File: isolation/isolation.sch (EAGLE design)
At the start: 81 parts, among them IC1 XTLV61048DBVR, IC2 SN74HC14DRG3, IC3 SN74HCS32PWR, IC4 SN74HCS08DYYR, IC5 FDN359BN, IC6 FDN359BN, IC7 FDN359BN, IC8 FDN359BN, J1 S4B-PH-K-S(LF)(SN), J2 S4B-PH-K-S(LF)(SN), J3 S4B-PH-K-S(LF)(SN), J4 S4B-PH-K-S(LF)(SN), J5 S4B-PH-K-S(LF)(SN)

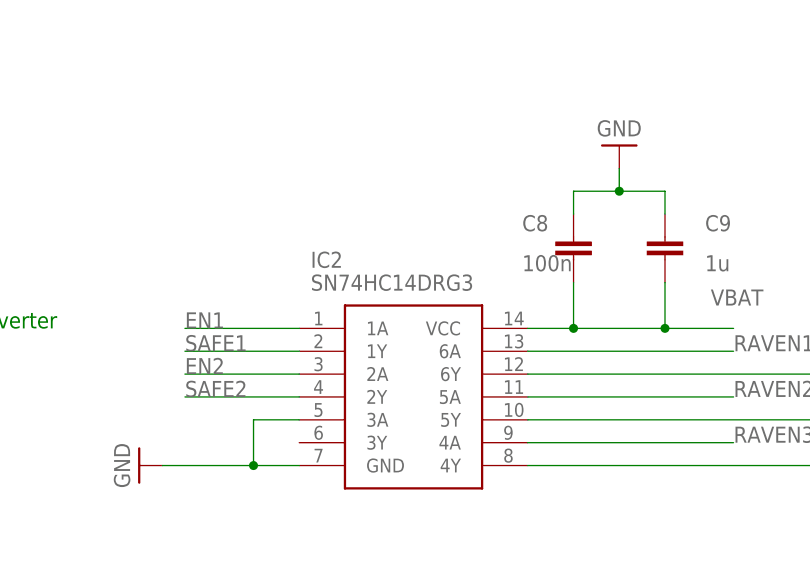
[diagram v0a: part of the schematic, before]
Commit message: move to smaller inverter
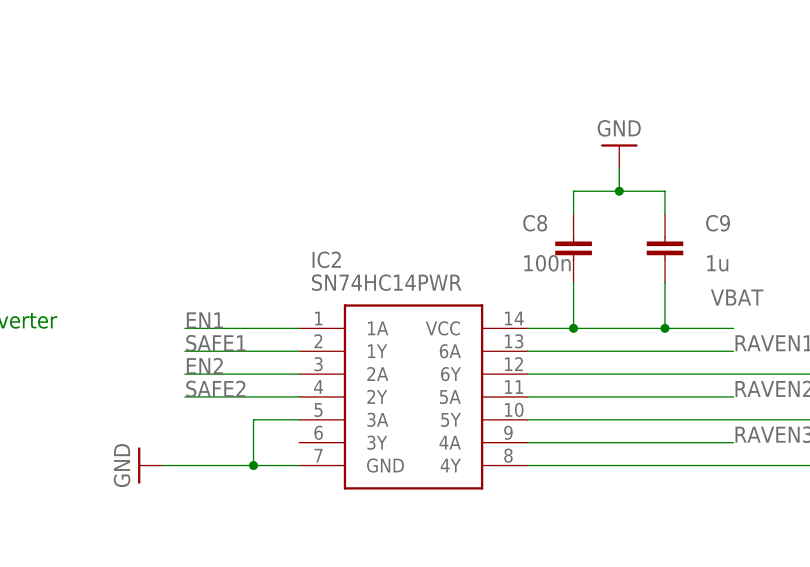
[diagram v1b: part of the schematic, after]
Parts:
- IC2: value SN74HC14DRG3 -> SN74HC14PWR; device SamacSys_Parts:SN74HC14DRG3 -> SamacSys_Parts:SN74HC14PWR
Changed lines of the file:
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@@
 <grid distance="0.1" unitdist="inch" unit="inch" style="lines" multiple="1" display="no" altdistance="0.01" altunitdist="inch" altunit="inch"/>
 <layers>
-<layer number="1" name="Top" color="4" fill="1" visible="no" active="no"/>
-<layer number="2" name="Route2" color="16" fill="1" visible="no" active="no"/>
-<layer number="3" name="Route3" color="17" fill="1" visible="no" active="no"/>
-<layer number="4" name="Route4" color="18" fill="1" visible="no" active="no"/>
-<layer number="5" name="Route5" color="19" fill="1" visible="no" active="no"/>
-<layer number="6" name="Route6" color="25" fill="1" visible="no" active="no"/>
-<layer number="7" name="Route7" color="26" fill="1" visible="no" active="no"/>
-<layer number="8" name="Route8" color="27" fill="1" visible="no" active="no"/>
-<layer number="9" name="Route9" color="28" fill="1" visible="no" active="no"/>
-<layer number="10" name="Route10" color="29" fill="1" visible="no" active="no"/>
-<layer number="11" name="Route11" color="30" fill="1" visible="no" active="no"/>
-<layer number="12" name="Route12" color="20" fill="1" visible="no" active="no"/>
-<layer number="13" name="Route13" color="21" fill="1" visible="no" active="no"/>
-<layer number="14" name="Route14" color="22" fill="1" visible="no" active="no"/>
-<layer number="15" name="Route15" color="23" fill="1" visible="no" active="no"/>
-<layer number="16" name="Bottom" color="1" fill="1" visible="no" active="no"/>
-<layer number="17" name="Pads" color="2" fill="1" visible="no" active="no"/>
-<layer number="18" name="Vias" color="2" fill="1" visible="no" active="no"/>
-<layer number="19" name="Unrouted" color="6" fill="1" visible="no" active="no"/>
-<layer number="20" name="Dimension" color="24" fill="1" visible="no" active="no"/>
-<layer number="21" name="tPlace" color="7" fill="1" visible="no" active="no"/>
-<layer number="22" name="bPlace" color="7" fill="1" visible="no" active="no"/>
-<layer number="23" name="tOrigins" color="15" fill="1" visible="no" active="no"/>
-<layer number="24" name="bOrigins" color="15" fill="1" visible="no" active="no"/>
-<layer number="25" name="tNames" color="7" fill="1" visible="no" active="no"/>
-<layer number="26" name="bNames" color="7" fill="1" visible="no" active="no"/>
-<layer number="27" name="tValues" color="7" fill="1" visible="no" active="no"/>
-<layer number="28" name="bValues" color="7" fill="1" visible="no" active="no"/>
+<layer number="1" name="Top" color="4" fill="1" visible="yes" active="no"/>
+<layer number="2" name="Route2" color="16" fill="1" visible="yes" active="no"/>
+<layer number="3" name="Route3" color="17" fill="1" visible="yes" active="no"/>
+<layer number="4" name="Route4" color="18" fill="1" visible="yes" active="no"/>
+<layer number="5" name="Route5" color="19" fill="1" visible="yes" active="no"/>
+<layer number="6" name="Route6" color="25" fill="1" visible="yes" active="no"/>
+<layer number="7" name="Route7" color="26" fill="1" visible="yes" active="no"/>
+<layer number="8" name="Route8" color="27" fill="1" visible="yes" active="no"/>
+<layer number="9" name="Route9" color="28" fill="1" visible="yes" active="no"/>
+<layer number="10" name="Route10" color="29" fill="1" visible="yes" active="no"/>
+<layer number="11" name="Route11" color="30" fill="1" visible="yes" active="no"/>
+<layer number="12" name="Route12" color="20" fill="1" visible="yes" active="no"/>
+<layer number="13" name="Route13" color="21" fill="1" visible="yes" active="no"/>
+<layer number="14" name="Route14" color="22" fill="1" visible="yes" active="no"/>
+<layer number="15" name="Route15" color="23" fill="1" visible="yes" active="no"/>
+<layer number="16" name="Bottom" color="1" fill="1" visible="yes" active="no"/>
+<layer number="17" name="Pads" color="2" fill="1" visible="yes" active="no"/>
+<layer number="18" name="Vias" color="2" fill="1" visible="yes" active="no"/>
+<layer number="19" name="Unrouted" color="6" fill="1" visible="yes" active="no"/>
+<layer number="20" name="Dimension" color="24" fill="1" visible="yes" active="no"/>
+<layer number="21" name="tPlace" color="7" fill="1" visible="yes" active="no"/>
+<layer number="22" name="bPlace" color="7" fill="1" visible="yes" active="no"/>
+<layer number="23" name="tOrigins" color="15" fill="1" visible="yes" active="no"/>
+<layer number="24" name="bOrigins" color="15" fill="1" visible="yes" active="no"/>
+<layer number="25" name="tNames" color="7" fill="1" visible="yes" active="no"/>
+<layer number="26" name="bNames" color="7" fill="1" visible="yes" active="no"/>
+<layer number="27" name="tValues" color="7" fill="1" visible="yes" active="no"/>
+<layer number="28" name="bValues" color="7" fill="1" visible="yes" active="no"/>
 <layer number="29" name="tStop" color="7" fill="3" visible="no" active="no"/>
 <layer number="30" name="bStop" color="7" fill="6" visible="no" active="no"/>
@@
 <layer number="35" name="tGlue" color="7" fill="4" visible="no" active="no"/>
 <layer number="36" name="bGlue" color="7" fill="5" visible="no" active="no"/>
-<layer number="37" name="tTest" color="7" fill="1" visible="no" active="no"/>
-<layer number="38" name="bTest" color="7" fill="1" visible="no" active="no"/>
+<layer number="37" name="tTest" color="7" fill="1" visible="yes" active="no"/>
+<layer number="38" name="bTest" color="7" fill="1" visible="yes" active="no"/>
 <layer number="39" name="tKeepout" color="4" fill="11" visible="no" active="no"/>
 <layer number="40" name="bKeepout" color="1" fill="11" visible="no" active="no"/>
@@
 <layer number="44" name="Drills" color="7" fill="1" visible="no" active="no"/>
 <layer number="45" name="Holes" color="7" fill="1" visible="no" active="no"/>
-<layer number="46" name="Milling" color="3" fill="1" visible="no" active="no"/>
-<layer number="47" name="Measures" color="7" fill="1" visible="no" active="no"/>
-<layer number="48" name="Document" color="7" fill="1" visible="no" active="no"/>
-<layer number="49" name="Reference" color="7" fill="1" visible="no" active="no"/>
-<layer number="50" name="dxf" color="7" fill="1" visible="no" active="no"/>
-<layer number="51" name="tDocu" color="7" fill="1" visible="no" active="no"/>
-<layer number="52" name="bDocu" color="7" fill="1" visible="no" active="no"/>
-<layer number="53" name="tGND_GNDA" color="7" fill="9" visible="no" active="no"/>
-<layer number="54" name="bGND_GNDA" color="1" fill="9" visible="no" active="no"/>
-<layer number="56" name="wert" color="7" fill="1" visible="no" active="no"/>
-<layer number="57" name="tCAD" color="7" fill="1" visible="no" active="no"/>
-<layer number="58" name="bCAD" color="11" fill="1" visible="no" active="no"/>
-<layer number="59" name="tCarbon" color="7" fill="1" visible="no" active="no"/>
-<layer number="60" name="bCarbon" color="7" fill="1" visible="no" active="no"/>
+<layer number="46" name="Milling" color="3" fill="1" visible="yes" active="no"/>
+<layer number="47" name="Measures" color="7" fill="1" visible="yes" active="no"/>
+<layer number="48" name="Document" color="7" fill="1" visible="yes" active="no"/>
+<layer number="49" name="Reference" color="7" fill="1" visible="yes" active="no"/>
+<layer number="50" name="dxf" color="7" fill="1" visible="yes" active="no"/>
+<layer number="51" name="tDocu" color="7" fill="1" visible="yes" active="no"/>
+<layer number="52" name="bDocu" color="7" fill="1" visible="yes" active="no"/>
+<layer number="53" name="tGND_GNDA" color="7" fill="9" visible="yes" active="no"/>
+<layer number="54" name="bGND_GNDA" color="1" fill="9" visible="yes" active="no"/>
+<layer number="56" name="wert" color="7" fill="1" visible="yes" active="no"/>
+<layer number="57" name="tCAD" color="7" fill="1" visible="yes" active="no"/>
+<layer number="58" name="bCAD" color="11" fill="1" visible="yes" active="no"/>
+<layer number="59" name="tCarbon" color="7" fill="1" visible="yes" active="no"/>
+<layer number="60" name="bCarbon" color="7" fill="1" visible="yes" active="no"/>
 <layer number="88" name="SimResults" color="9" fill="1" visible="yes" active="yes"/>
 <layer number="89" name="SimProbes" color="9" fill="1" visible="yes" active="yes"/>
@@
 <part name="E1" library="SamacSys_Parts" deviceset="SJ1-3525N" device=""/>
 <part name="SUPPLY8" library="Power_Symbols" library_urn="urn:adsk.eagle:library:16502351" deviceset="GND-BAR" device="" value="GND"/>
-<part name="IC2" library="SamacSys_Parts" deviceset="SN74HC14DRG3" device=""/>
+<part name="IC2" library="SamacSys_Parts" deviceset="SN74HC14PWR" device=""/>
 <part name="SUPPLY9" library="Power_Symbols" library_urn="urn:adsk.eagle:library:16502351" deviceset="GND-BAR" device="" value="GND"/>
 <part name="SUPPLY10" library="Power_Symbols" library_urn="urn:adsk.eagle:library:16502351" deviceset="GND-BAR" device="" value="GND"/>

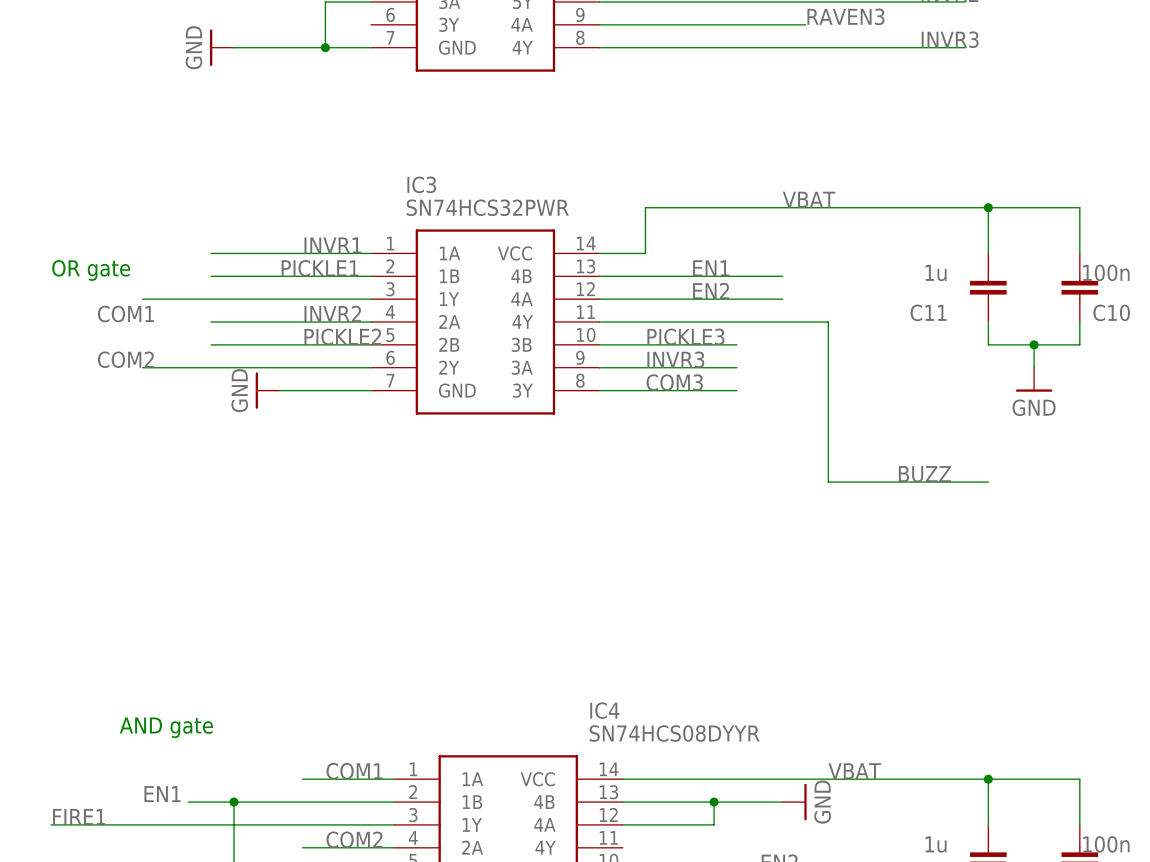
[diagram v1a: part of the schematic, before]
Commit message: smaller OR IC
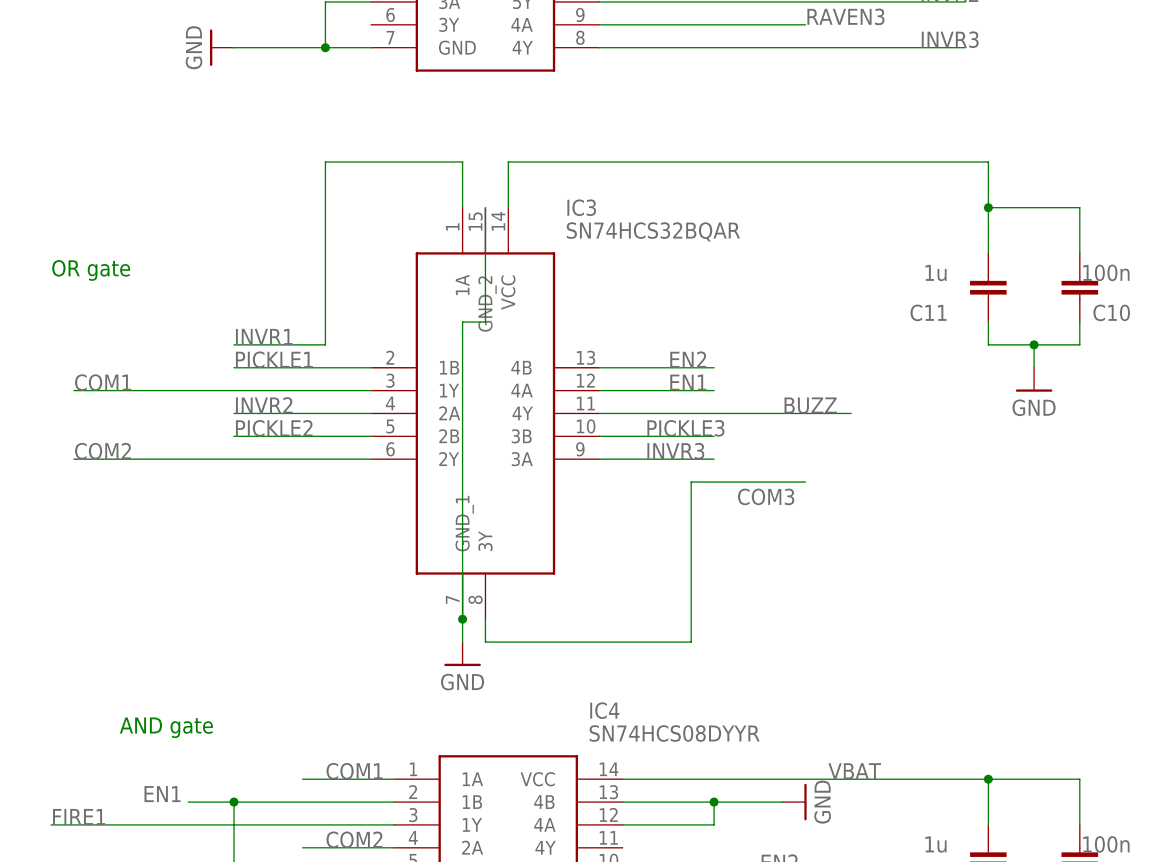
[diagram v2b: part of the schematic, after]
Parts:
- IC3: value SN74HCS32PWR -> SN74HCS32BQAR; device SamacSys_Parts:SN74HCS32PWR -> SamacSys_Parts:SN74HCS32BQAR
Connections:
- net EN1: now also IC3.4A; no longer IC3.4B
- net EN2: now also IC3.4B; no longer IC3.4A
- net GND: now also IC3.GND_1, IC3.GND_2; no longer IC3.GND
